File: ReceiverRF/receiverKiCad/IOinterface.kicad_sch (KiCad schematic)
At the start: 19 parts, among them Q1 MMBT3904, SW1 SW_Push, SW2 SW_Push, SW3 SW_Push, SW4 SW_Push

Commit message: changement vers footprint 1206
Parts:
- BUT_R1, BUT_R2, BUT_R4, BUZ_R2: footprint Resistor_SMD:R_0402_1005Metric -> Resistor_SMD:R_1206_3216Metric
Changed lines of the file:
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@@
 			)
 		)
-		(property "Footprint" "Resistor_SMD:R_0402_1005Metric"
+		(property "Footprint" "Resistor_SMD:R_1206_3216Metric"
 			(at 39.37 76.708 90)
 			(effects
@@
 			)
 		)
-		(property "Footprint" "Resistor_SMD:R_0402_1005Metric"
+		(property "Footprint" "Resistor_SMD:R_1206_3216Metric"
 			(at 106.172 39.37 90)
 			(effects
@@
 			)
 		)
-		(property "Footprint" "Resistor_SMD:R_0402_1005Metric"
+		(property "Footprint" "Resistor_SMD:R_1206_3216Metric"
 			(at 106.172 74.93 90)
 			(effects
@@
 			)
 		)
-		(property "Footprint" "Resistor_SMD:R_0402_1005Metric"
+		(property "Footprint" "Resistor_SMD:R_1206_3216Metric"
 			(at 82.042 39.37 90)
 			(effects

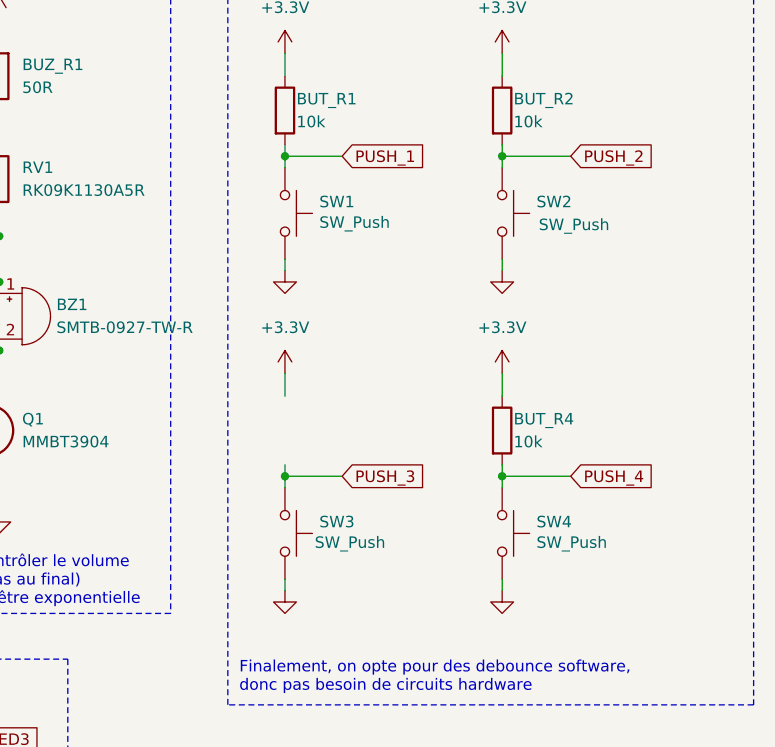
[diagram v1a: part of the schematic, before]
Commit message: changement BOM et choix nouvelles pièces 1206
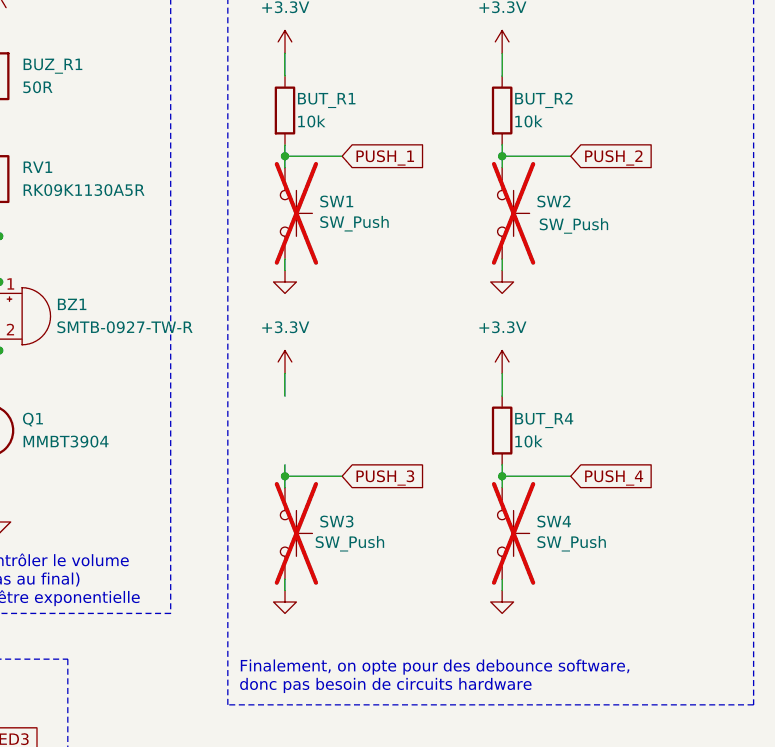
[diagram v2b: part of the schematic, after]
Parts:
- BUT_R1, BUT_R2, BUT_R4: Digikey 311-10KJRCT-ND -> 311-10.0KFRCT-ND
- BUZ_R2: Digikey P1.5KDCCT-ND -> 541-4184-1-ND
- RV1: Digikey (none) -> PTV09A-4025S-A103-ND
- SW1, SW2, SW3, SW4: now not fitted
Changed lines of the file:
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@@
 		(in_bom yes)
 		(on_board yes)
-		(dnp no)
+		(dnp yes)
 		(property "Reference" "SW3"
 			(at 87.63 85.09 90)
@@
 		(in_bom yes)
 		(on_board yes)
-		(dnp no)
+		(dnp yes)
 		(property "Reference" "SW2"
 			(at 111.76 49.53 90)
@@
 			)
 		)
-		(property "Digikey" "P1.5KDCCT-ND"
+		(property "Digikey" "541-4184-1-ND"
 			(at 39.37 74.93 0)
 			(effects
@@
 			)
 		)
-		(property "Digikey" "311-10KJRCT-ND"
+		(property "Digikey" "311-10.0KFRCT-ND"
 			(at 107.95 39.37 0)
 			(effects
@@
 			)
 		)
-		(property "Digikey" "311-10KJRCT-ND"
+		(property "Digikey" "311-10.0KFRCT-ND"
 			(at 107.95 74.93 0)
 			(effects
@@
 			)
 		)
-		(property "Digikey" ""
+		(property "Digikey" "PTV09A-4025S-A103-ND"
 			(at 52.07 46.99 0)
 			(effects
@@
 		(in_bom yes)
 		(on_board yes)
-		(dnp no)
+		(dnp yes)
 		(property "Reference" "SW1"
 			(at 87.63 49.53 90)
@@
 		(in_bom yes)
 		(on_board yes)
-		(dnp no)
+		(dnp yes)
 		(property "Reference" "SW4"
 			(at 111.76 85.09 90)
@@
 			)
 		)
-		(property "Digikey" "311-10KJRCT-ND"
+		(property "Digikey" "311-10.0KFRCT-ND"
 			(at 83.82 39.37 0)
 			(effects

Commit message: firmware oscillateur interne :(
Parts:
- added BUT_R3: 10k, Resistor_SMD:R_1206_3216Metric, symbol Device:R
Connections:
- net +3.3V: now also BUT_R3.1
- net PUSH_3: now also BUT_R3.2
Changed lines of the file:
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@@
+	)
+	(symbol
+		(lib_id "Device:R")
+		(at 83.82 74.93 0)
+		(unit 1)
+		(exclude_from_sim no)
+		(in_bom yes)
+		(on_board yes)
+		(dnp no)
+		(property "Reference" "BUT_R3"
+			(at 85.09 73.66 0)
+			(effects
+				(font
+					(size 1.27 1.27)
+				)
+				(justify left)
+			)
+		)
+		(property "Value" "10k"
+			(at 85.09 76.2 0)
+			(effects
+				(font
+					(size 1.27 1.27)
+				)
+				(justify left)
+			)
+		)
+		(property "Footprint" "Resistor_SMD:R_1206_3216Metric"
+			(at 82.042 74.93 90)
+			(effects
+				(font
+					(size 1.27 1.27)
+				)
+				(hide yes)
+			)
+		)
+		(property "Datasheet" "~"
+			(at 83.82 74.93 0)
+			(effects
+				(font
+					(size 1.27 1.27)
+				)
+				(hide yes)
+			)
+		)
+		(property "Description" ""
+			(at 83.82 74.93 0)
+			(effects
+				(font
+					(size 1.27 1.27)
+				)
+				(hide yes)
+			)
+		)
+		(property "Digikey" "311-10.0KFRCT-ND"
+			(at 83.82 74.93 0)
+			(effects
+				(font
+					(size 1.27 1.27)
+				)
+				(hide yes)
+			)
+		)
+		(pin "1"
+		)
+		(pin "2"
+		)
+		(instances
+			(project "receiver"
+				(path "/439ba515-58d4-4b14-87ab-b438dcf423a5/4d4f24f8-ecba-4dd7-9441-941d52592651"
+					(reference "BUT_R3")
+					(unit 1)
+				)
+			)
+		)
 	)
 	(symbol

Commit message: ideFIX v2 fix schematic, layout
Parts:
- removed D1, D2, D3: LTST-C170GKT, Footprints:LTST-C170GKT, symbol Device:LED
- removed LED_R1, LED_R2, LED_R3: 145R, Resistor_SMD:R_1206_3216Metric, symbol Device:R
- added IF1, IF2: ~, Footprints:CONN10_530481010_MOL, symbol Symboles:INTERFACE_BOARD
- added J4: Conn_01x04, Connector_PinHeader_2.54mm:PinHeader_1x04_P2.54mm_Vertical, symbol Connector_Generic:Conn_01x04
- added LLS_C1, LLS_C2: 100nF, Capacitor_SMD:C_1206_3216Metric, symbol Device:C
- added LLS_R2: 10k, Resistor_SMD:R_1206_3216Metric, symbol Device:R
- added U5: TXS0102DCUR, Footprints:SOP50P310X90-8N, symbol Symboles:TXS0102DCUR
- SW1, SW2, SW3, SW4: now fitted
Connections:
- net +3.3V: now also IF1.9 (P9); no longer BUT_R1.1, BUT_R2.1, BUT_R3.1, BUT_R4.1
- net +5V: now also IF1.10 (P10); no longer BUZ_R1.2
- net BUZZER: now also IF1.8 (P8); no longer BUZ_R2.1
- net GND: now also IF1.1 (P1); no longer Q1.3 (E), SW1.2, SW2.2, SW3.2, SW4.2
- net PUSH_1: now also IF1.5 (P5); no longer BUT_R1.2, SW1.1
- net PUSH_2: now also IF1.4 (P4); no longer BUT_R2.2, SW2.1
- net PUSH_3: now also IF1.3 (P3); no longer BUT_R3.2, SW3.1
- net PUSH_4: now also IF1.2 (P2); no longer BUT_R4.2, SW4.1
- new net: J4.3 (SDA), U5.8 (B1)
- new net: J4.4 (SCL), U5.1 (B2)
- new net +3.3V_IB: BUT_R1.1, BUT_R2.1, BUT_R3.1, BUT_R4.1, IF2.2 (P2), LLS_C1.2, LLS_R2.1, U5.3 (VCCA), U5.6 (OE)
- new net +5V_IB: BUZ_R1.2, IF2.1 (P1), J4.2 (VCC), LLS_C2.2, U5.7 (VCCB)
- new net BUZZER_IB: BUZ_R2.1, IF2.3 (P3)
- new net GND_IB: IF2.10 (P10), J4.1 (GND), LLS_C1.1, LLS_C2.1, LLS_R2.2, Q1.3 (E), SW1.2, SW2.2, SW3.2, SW4.2, U5.2 (GND)
- new net I2C_SCL: IF1.6 (P6)
- new net I2C_SCL_IB: IF2.5 (P5), U5.4 (A2)
- new net I2C_SDA: IF1.7 (P7)
- new net I2C_SDA_IB: IF2.4 (P4), U5.5 (A1)
- new net PUSH_1_IB: BUT_R1.2, IF2.6 (P6), SW1.1
- new net PUSH_2_IB: BUT_R2.2, IF2.7 (P7), SW2.1
- new net PUSH_3_IB: BUT_R3.2, IF2.8 (P8), SW3.1
- new net PUSH_4_IB: BUT_R4.2, IF2.9 (P9), SW4.1
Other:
- note added: "Connection main-board / interface-board"
- note added: "L'Enable est active HIGH"
- note added: "L'écran LCD est hors du PCB. On le connectera avec des jumpers ou un bus à quatres fils."
- note added: "Logic level shifter pour passer du I2C 3V3 à 5V"
- note added: "Écran LCD 4x20"
- note removed: "Ces LED tirent 10mA chacunes"
- note removed: "LED d'état"
- moved on the sheet: BUT_R1, BUT_R2, BUT_R3, BUT_R4, BUZ_D1, BUZ_R1, BUZ_R2, BZ1, Q1, RV1

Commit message: revision schematic before tracing
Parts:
- SW1, SW2, SW3, SW4: Digikey (none) -> EG1862-ND
- U5: Digikey (none) -> 296-21931-2-ND
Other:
- company: (none) -> GAUL
- title: (none) -> IdeFIX
- moved on the sheet: BUT_R1, BUT_R2, BUT_R3, BUT_R4, SW1, SW2, SW3, SW4

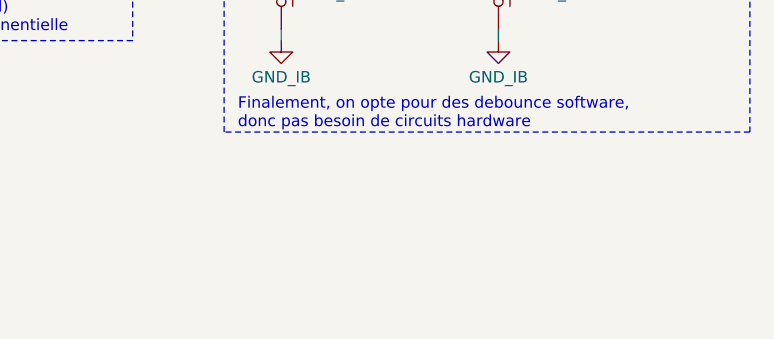
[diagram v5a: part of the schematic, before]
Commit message: 3.2mm holes, XT30 connector, add polyfuse, minor fixes
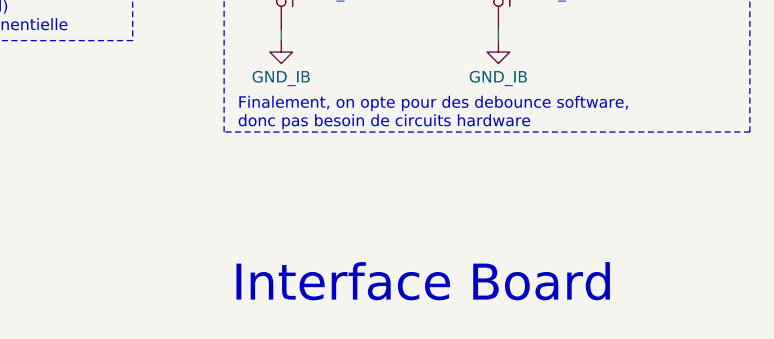
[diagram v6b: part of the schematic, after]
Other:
- note added: "Interface Board"
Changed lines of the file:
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@@
+		)
+	)
+	(text "Interface Board"
+		(exclude_from_sim no)
+		(at 202.438 171.958 0)
+		(effects
+			(font
+				(size 4 4)
+			)
 		)
 	)

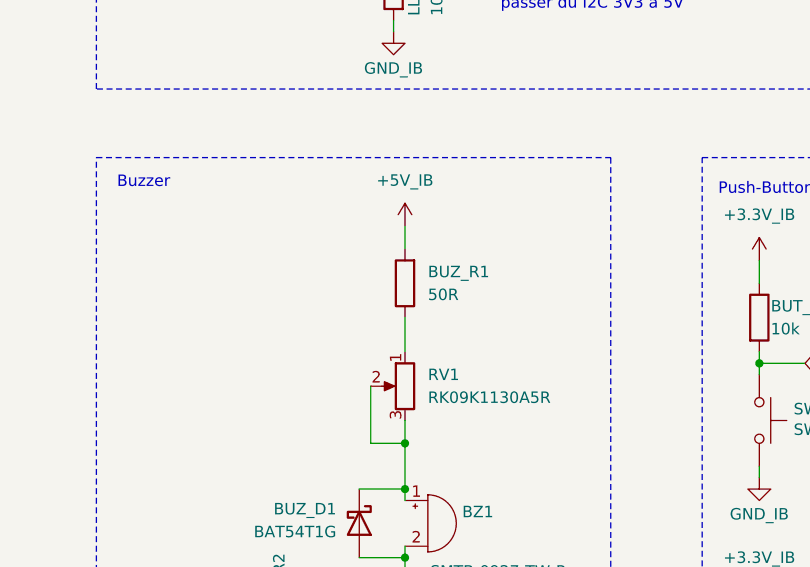
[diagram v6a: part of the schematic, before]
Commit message: Refactor timer handling and add TRANSMIT/RECEIVE definition macros
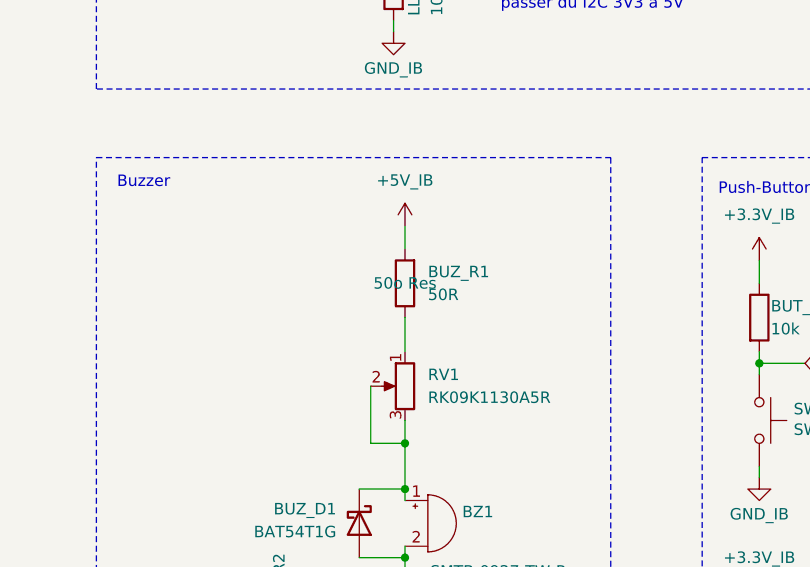
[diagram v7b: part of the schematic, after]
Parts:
- J4: now left out of the parts list
- RV1: Digikey PTV09A-4025S-A103-ND -> 4809-RK09K1130A5R-ND
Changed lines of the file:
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@@
 		(unit 1)
 		(exclude_from_sim no)
-		(in_bom yes)
+		(in_bom no)
 		(on_board yes)
 		(dnp no)
@@
 			)
 		)
-		(property "Description" ""
+		(property "Description" "50o Res"
 			(at 147.32 85.09 0)
 			(effects
@@
 			)
 		)
-		(property "Description" ""
+		(property "Description" "10k Res"
 			(at 186.69 127 0)
 			(effects
@@
 			)
 		)
-		(property "Description" ""
+		(property "Description" "PCB connector"
 			(at 49.53 45.72 0)
 			(effects
@@
 			)
 		)
-		(property "Description" ""
+		(property "Description" "100nF Cap"
 			(at 189.23 29.21 0)
 			(effects
@@
 			)
 		)
-		(property "Description" "SMTB-0927-TW-R"
+		(property "Description" "Buzzer"
 			(at 149.86 111.76 0)
 			(effects
@@
 			)
 		)
-		(property "Description" ""
+		(property "Description" "100nF Cap"
 			(at 147.32 29.21 0)
 			(effects
@@
 			)
 		)
-		(property "Description" ""
+		(property "Description" "Button"
 			(at 186.69 138.43 0)
 			(effects
@@
 			)
 		)
-		(property "Description" ""
+		(property "Description" "10k Res"
 			(at 146.05 52.07 0)
 			(effects
@@
 			)
 		)
-		(property "Description" ""
+		(property "Description" "Button"
 			(at 210.82 100.33 0)
 			(effects
@@
 			)
 		)
-		(property "Description" ""
+		(property "Description" "Logic level shifter"
 			(at 190.5 38.1 0)
 			(effects
@@
 			)
 		)
-		(property "Description" ""
+		(property "Description" "1k5 Res"
 			(at 134.62 124.46 0)
 			(effects
@@
 			)
 		)
-		(property "Description" ""
+		(property "Description" "PCB connector"
 			(at 69.85 43.18 0)
 			(effects
@@
 			)
 		)
-		(property "Description" ""
+		(property "Description" "10k Res"
 			(at 210.82 88.9 0)
 			(effects
@@
 			)
 		)
-		(property "Description" ""
+		(property "Description" "10k Res"
 			(at 210.82 127 0)
 			(effects
@@
 			)
 		)
-		(property "Description" "RK09K1130A5R"
+		(property "Description" "Potentiometer"
 			(at 147.32 96.52 0)
 			(effects
@@
 			)
 		)
-		(property "Digikey" "PTV09A-4025S-A103-ND"
+		(property "Digikey" "  4809-RK09K1130A5R-ND"
 			(at 147.32 96.52 0)
 			(effects
@@
 			)
 		)
-		(property "Description" ""
+		(property "Description" "Schottky diode"
 			(at 142.24 111.76 0)
 			(effects
@@
 			)
 		)
-		(property "Description" ""
+		(property "Description" "Button"
 			(at 186.69 100.33 0)
 			(effects
@@
 			)
 		)
-		(property "Description" ""
+		(property "Description" "Button"
 			(at 210.82 138.43 0)
 			(effects
@@
 			)
 		)
-		(property "Description" ""
+		(property "Description" "10k Res"
 			(at 186.69 88.9 0)
 			(effects
